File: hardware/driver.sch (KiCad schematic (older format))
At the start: 15 parts, among them Q1 BSS84, Q2 BSS138, Q3 BSS138, Q4 BSS84, Q5 BSS138, Q6 BSS138

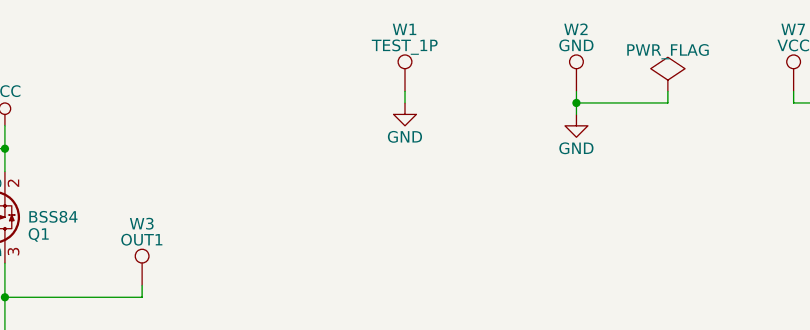
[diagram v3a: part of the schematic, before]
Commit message: Assigned footprints
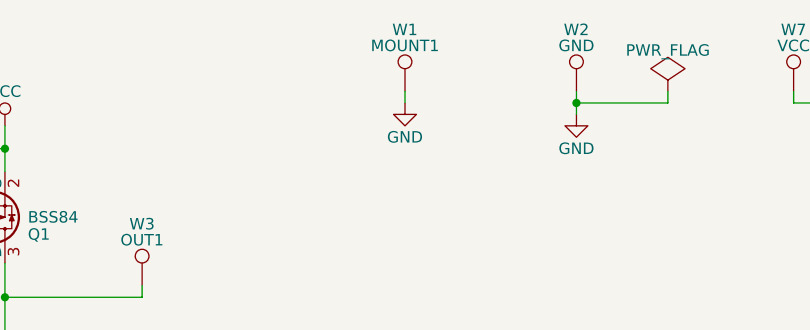
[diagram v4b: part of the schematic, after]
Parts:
- Q1, Q4: footprint (none) -> TO_SOT_Packages_SMD:SOT-23
- W1: value TEST_1P -> MOUNT1; footprint (none) -> Mounting_Holes:MountingHole_2.5mm_Pad
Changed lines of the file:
@@
 F 0 "Q1" H 4650 2175 50  0000 L CNN
 F 1 "BSS84" H 4650 2100 50  0000 L CNN
-F 2 "" H 4650 2025 50  0000 L CIN
+F 2 "TO_SOT_Packages_SMD:SOT-23" H 4650 2025 50  0001 L CIN
 F 3 "" H 4650 2175 50  0000 L CNN
 	1    4450 2100
@@
 F 0 "R1" V 3580 2150 50  0000 C CNN
 F 1 "R" V 3500 2150 50  0000 C CNN
-F 2 "" V 3430 2150 50  0000 C CNN
+F 2 "" V 3430 2150 50  0001 C CNN
 F 3 "" H 3500 2150 50  0000 C CNN
 	1    3500 2150
@@
 F 0 "W4" H 3000 3070 50  0000 C CNN
 F 1 "IN1" H 3000 3000 50  0000 C CNN
-F 2 "" H 3200 2800 50  0000 C CNN
+F 2 "" H 3200 2800 50  0001 C CNN
 F 3 "" H 3200 2800 50  0000 C CNN
 	1    3000 2800
@@
 F 0 "Q4" H 4650 4225 50  0000 L CNN
 F 1 "BSS84" H 4650 4150 50  0000 L CNN
-F 2 "" H 4650 4075 50  0000 L CIN
+F 2 "TO_SOT_Packages_SMD:SOT-23" H 4650 4075 50  0001 L CIN
 F 3 "" H 4650 4225 50  0000 L CNN
 	1    4450 4150
@@
 F 0 "R2" V 3580 4200 50  0000 C CNN
 F 1 "R" V 3500 4200 50  0000 C CNN
-F 2 "" V 3430 4200 50  0000 C CNN
+F 2 "" V 3430 4200 50  0001 C CNN
 F 3 "" H 3500 4200 50  0000 C CNN
 	1    3500 4200
@@
 F 0 "W6" H 3000 5120 50  0000 C CNN
 F 1 "IN2" H 3000 5050 50  0000 C CNN
-F 2 "" H 3200 4850 50  0000 C CNN
+F 2 "" H 3200 4850 50  0001 C CNN
 F 3 "" H 3200 4850 50  0000 C CNN
 	1    3000 4850
@@
 F 0 "W5" H 5150 4720 50  0000 C CNN
 F 1 "OUT2" H 5150 4650 50  0000 C CNN
-F 2 "" H 5350 4450 50  0000 C CNN
+F 2 "" H 5350 4450 50  0001 C CNN
 F 3 "" H 5350 4450 50  0000 C CNN
 	1    5150 4450
@@
 F 0 "W3" H 5150 2670 50  0000 C CNN
 F 1 "OUT1" H 5150 2600 50  0000 C CNN
-F 2 "" H 5350 2400 50  0000 C CNN
+F 2 "" H 5350 2400 50  0001 C CNN
 F 3 "" H 5350 2400 50  0000 C CNN
 	1    5150 2400
@@
 P 6300 1550
 F 0 "W1" H 6300 1820 50  0000 C CNN
-F 1 "TEST_1P" H 6300 1750 50  0000 C CNN
-F 2 "" H 6500 1550 50  0000 C CNN
+F 1 "MOUNT1" H 6300 1750 50  0000 C CNN
+F 2 "Mounting_Holes:MountingHole_2.5mm_Pad" H 6500 1550 50  0001 C CNN
 F 3 "" H 6500 1550 50  0000 C CNN
 	1    6300 1550
@@
 F 0 "W2" H 7050 1820 50  0000 C CNN
 F 1 "GND" H 7050 1750 50  0000 C CNN
-F 2 "" H 7250 1550 50  0000 C CNN
+F 2 "" H 7250 1550 50  0001 C CNN
 F 3 "" H 7250 1550 50  0000 C CNN
 	1    7050 1550
@@
 F 0 "W7" H 8000 1820 50  0000 C CNN
 F 1 "VCC" H 8000 1750 50  0000 C CNN
-F 2 "" H 8200 1550 50  0000 C CNN
+F 2 "" H 8200 1550 50  0001 C CNN
 F 3 "" H 8200 1550 50  0000 C CNN
 	1    8000 1550

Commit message: Initial PCB layout
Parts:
- R1, R2: footprint (none) -> Resistors_SMD:R_0603_HandSoldering
- W2, W3, W4, W5, W6, W7: footprint (none) -> Measurement_Points:Measurement_Point_Square-TH_Big
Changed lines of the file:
@@
 F 0 "R1" V 3580 2150 50  0000 C CNN
 F 1 "R" V 3500 2150 50  0000 C CNN
-F 2 "" V 3430 2150 50  0001 C CNN
+F 2 "Resistors_SMD:R_0603_HandSoldering" V 3430 2150 50  0001 C CNN
 F 3 "" H 3500 2150 50  0000 C CNN
 	1    3500 2150
@@
 F 0 "W4" H 3000 3070 50  0000 C CNN
 F 1 "IN1" H 3000 3000 50  0000 C CNN
-F 2 "" H 3200 2800 50  0001 C CNN
+F 2 "Measurement_Points:Measurement_Point_Square-TH_Big" H 3200 2800 50  0001 C CNN
 F 3 "" H 3200 2800 50  0000 C CNN
 	1    3000 2800
@@
 F 0 "R2" V 3580 4200 50  0000 C CNN
 F 1 "R" V 3500 4200 50  0000 C CNN
-F 2 "" V 3430 4200 50  0001 C CNN
+F 2 "Resistors_SMD:R_0603_HandSoldering" V 3430 4200 50  0001 C CNN
 F 3 "" H 3500 4200 50  0000 C CNN
 	1    3500 4200
@@
 F 0 "W6" H 3000 5120 50  0000 C CNN
 F 1 "IN2" H 3000 5050 50  0000 C CNN
-F 2 "" H 3200 4850 50  0001 C CNN
+F 2 "Measurement_Points:Measurement_Point_Square-TH_Big" H 3200 4850 50  0001 C CNN
 F 3 "" H 3200 4850 50  0000 C CNN
 	1    3000 4850
@@
 F 0 "W5" H 5150 4720 50  0000 C CNN
 F 1 "OUT2" H 5150 4650 50  0000 C CNN
-F 2 "" H 5350 4450 50  0001 C CNN
+F 2 "Measurement_Points:Measurement_Point_Square-TH_Big" H 5350 4450 50  0001 C CNN
 F 3 "" H 5350 4450 50  0000 C CNN
 	1    5150 4450
@@
 F 0 "W3" H 5150 2670 50  0000 C CNN
 F 1 "OUT1" H 5150 2600 50  0000 C CNN
-F 2 "" H 5350 2400 50  0001 C CNN
+F 2 "Measurement_Points:Measurement_Point_Square-TH_Big" H 5350 2400 50  0001 C CNN
 F 3 "" H 5350 2400 50  0000 C CNN
 	1    5150 2400
@@
 F 0 "W2" H 7050 1820 50  0000 C CNN
 F 1 "GND" H 7050 1750 50  0000 C CNN
-F 2 "" H 7250 1550 50  0001 C CNN
+F 2 "Measurement_Points:Measurement_Point_Square-TH_Big" H 7250 1550 50  0001 C CNN
 F 3 "" H 7250 1550 50  0000 C CNN
 	1    7050 1550
@@
 F 0 "W7" H 8000 1820 50  0000 C CNN
 F 1 "VCC" H 8000 1750 50  0000 C CNN
-F 2 "" H 8200 1550 50  0001 C CNN
+F 2 "Measurement_Points:Measurement_Point_Square-TH_Big" H 8200 1550 50  0001 C CNN
 F 3 "" H 8200 1550 50  0000 C CNN
 	1    8000 1550

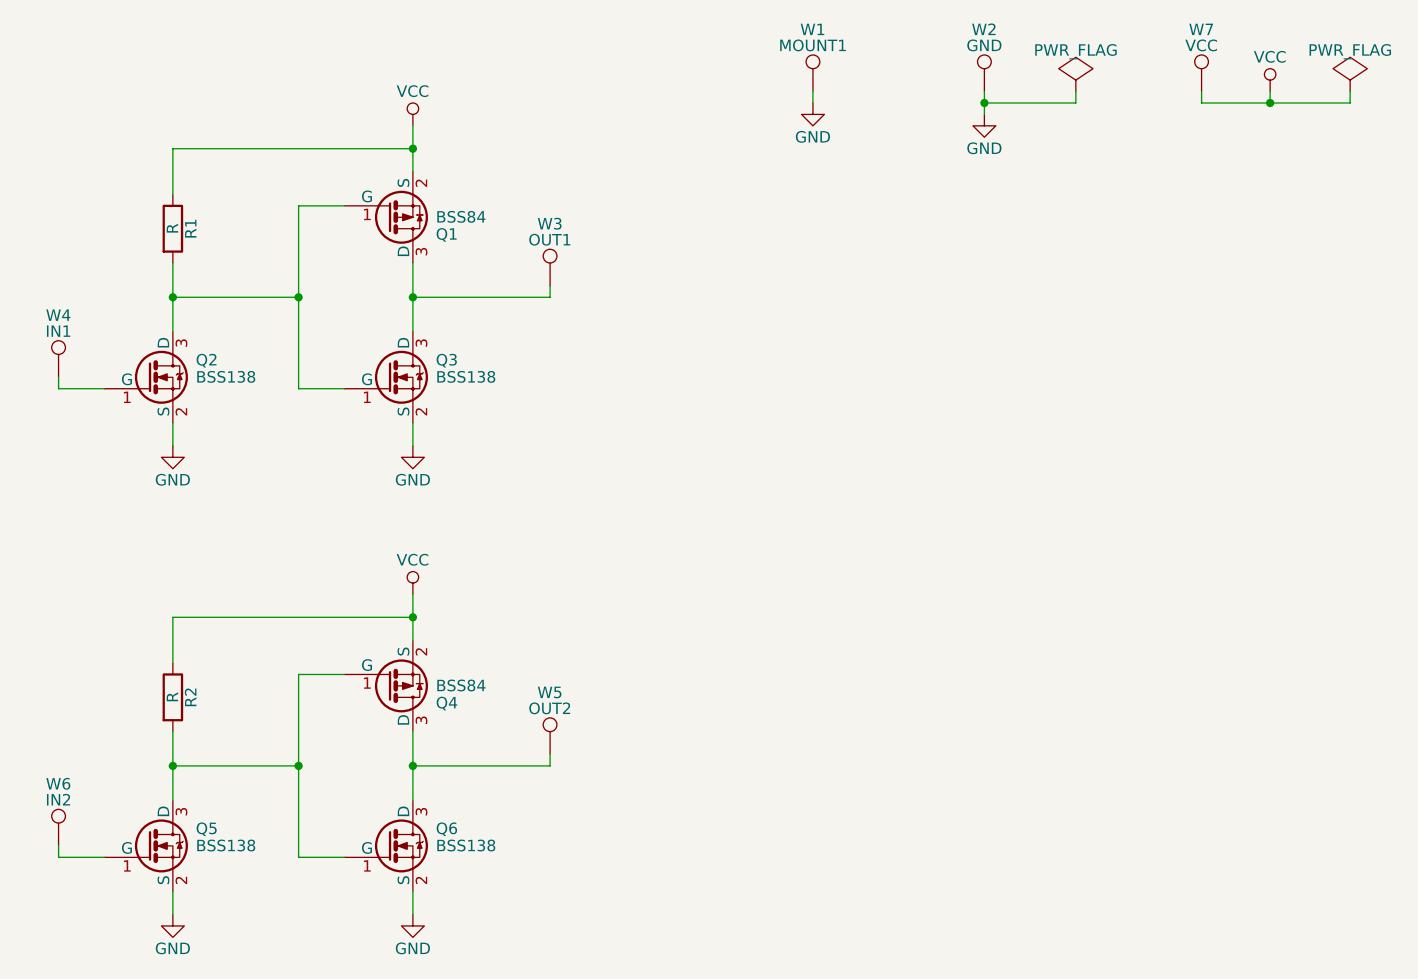
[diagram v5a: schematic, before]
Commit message: Added optional RC filter
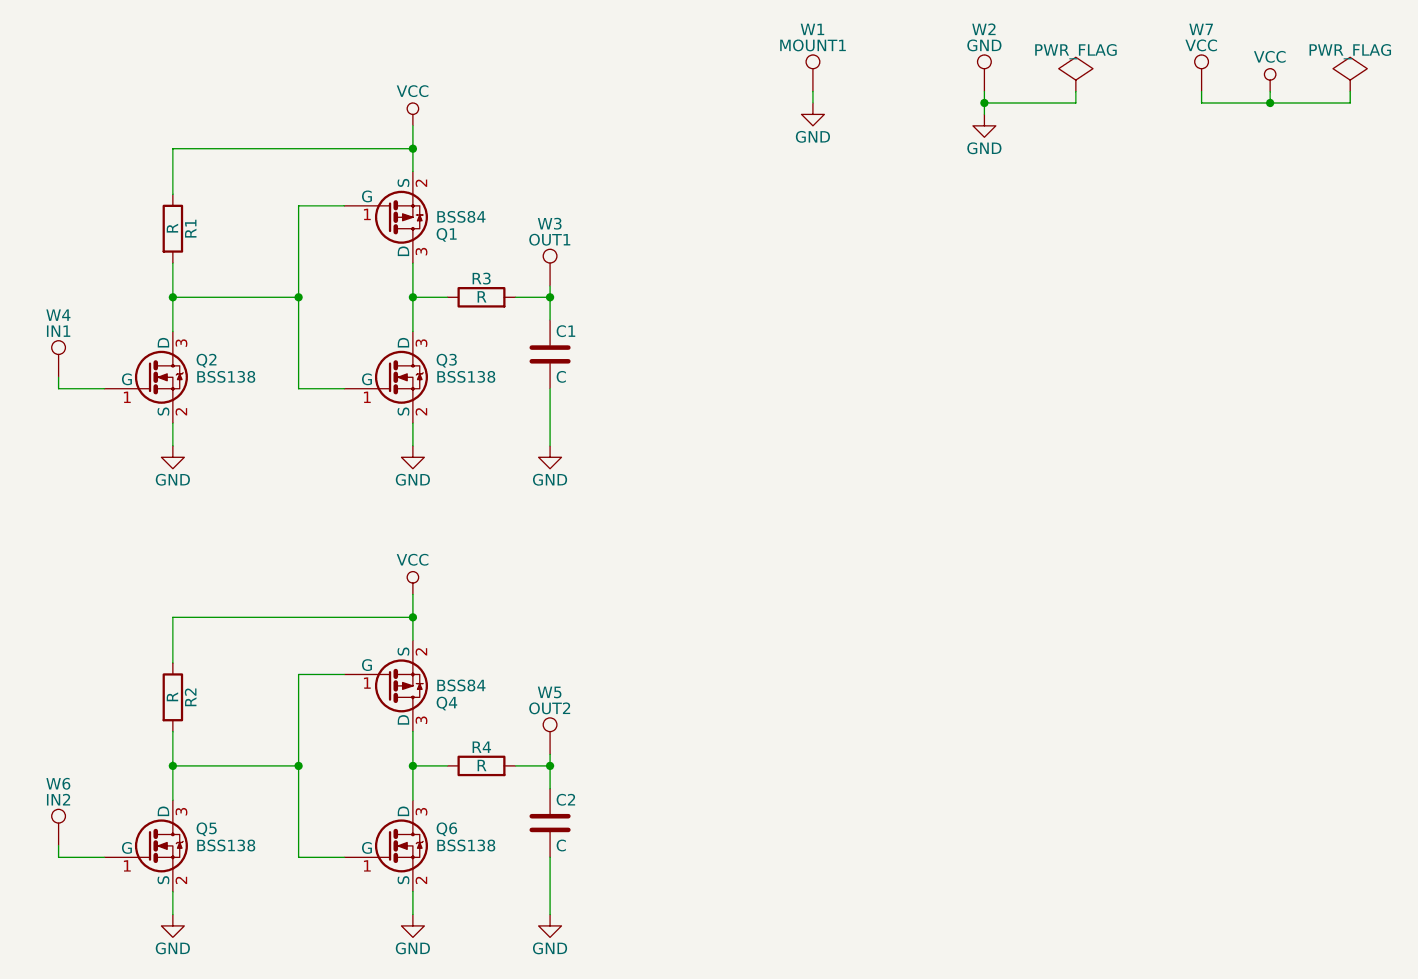
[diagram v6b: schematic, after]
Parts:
- added C1, C2: C, Capacitors_SMD:C_0603_HandSoldering, symbol C
- added R3, R4: R, Resistors_SMD:R_0603_HandSoldering, symbol R
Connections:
- net GND: now also C1.2, C2.2
- net at Q1.3 (D), Q3.3 (D): now also R3.1; no longer W3.1
- net at Q4.3 (D), Q6.3 (D): now also R4.1; no longer W5.1
- new net: C2.1, R4.2, W5.1
- new net: C1.1, R3.2, W3.1
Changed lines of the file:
@@
 Connection ~ 4050 2450
 Connection ~ 3500 2450
-Wire Wire Line
-	4550 2450 5150 2450
 Connection ~ 4550 2450
 Wire Wire Line
@@
 	1    0    0    1
 $EndComp
-Wire Wire Line
-	4550 4500 5150 4500
 Connection ~ 4550 4500
 $Comp
@@
 $EndComp
 Wire Wire Line
-	5150 2450 5150 2400
-Wire Wire Line
-	5150 4500 5150 4450
+	5150 2400 5150 2550
+Wire Wire Line
+	5150 4450 5150 4600
 Wire Wire Line
 	4550 2300 4550 2600
@@
 	7450 1600 7450 1550
 Connection ~ 7050 1600
+$Comp
+L R R3
+U 1 1 58938045
+P 4850 2450
+F 0 "R3" V 4930 2450 50  0000 C CNN
+F 1 "R" V 4850 2450 50  0000 C CNN
+F 2 "Resistors_SMD:R_0603_HandSoldering" V 4780 2450 50  0001 C CNN
+F 3 "" H 4850 2450 50  0000 C CNN
+	1    4850 2450
+	0    -1   -1   0
+$EndComp
+Wire Wire Line
+	4550 2450 4700 2450
+Wire Wire Line
+	5000 2450 5150 2450
+$Comp
+L R R4
+U 1 1 58938378
+P 4850 4500
+F 0 "R4" V 4930 4500 50  0000 C CNN
+F 1 "R" V 4850 4500 50  0000 C CNN
+F 2 "Resistors_SMD:R_0603_HandSoldering" V 4780 4500 50  0001 C CNN
+F 3 "" H 4850 4500 50  0000 C CNN
+	1    4850 4500
+	0    -1   -1   0
+$EndComp
+Wire Wire Line
+	4700 4500 4550 4500
+Wire Wire Line
+	5000 4500 5150 4500
+$Comp
+L C C1
+U 1 1 58938479
+P 5150 2700
+F 0 "C1" H 5175 2800 50  0000 L CNN
+F 1 "C" H 5175 2600 50  0000 L CNN
+F 2 "Capacitors_SMD:C_0603_HandSoldering" H 5188 2550 50  0001 C CNN
+F 3 "" H 5150 2700 50  0000 C CNN
+	1    5150 2700
+	1    0    0    -1
+$EndComp
+$Comp
+L C C2
+U 1 1 589389FC
+P 5150 4750
+F 0 "C2" H 5175 4850 50  0000 L CNN
+F 1 "C" H 5175 4650 50  0000 L CNN
+F 2 "Capacitors_SMD:C_0603_HandSoldering" H 5188 4600 50  0001 C CNN
+F 3 "" H 5150 4750 50  0000 C CNN
+	1    5150 4750
+	1    0    0    -1
+$EndComp
+Connection ~ 5150 2450
+$Comp
+L GND #PWR012
+U 1 1 589397B2
+P 5150 3100
+F 0 "#PWR012" H 5150 2850 50  0001 C CNN
+F 1 "GND" H 5150 2950 50  0000 C CNN
+F 2 "" H 5150 3100 50  0000 C CNN
+F 3 "" H 5150 3100 50  0000 C CNN
+	1    5150 3100
+	1    0    0    -1
+$EndComp
+Wire Wire Line
+	5150 2850 5150 3100
+Connection ~ 5150 4500
+Wire Wire Line
+	5150 4900 5150 5150
+$Comp
+L GND #PWR013
+U 1 1 58939E89
+P 5150 5150
+F 0 "#PWR013" H 5150 4900 50  0001 C CNN
+F 1 "GND" H 5150 5000 50  0000 C CNN
+F 2 "" H 5150 5150 50  0000 C CNN
+F 3 "" H 5150 5150 50  0000 C CNN
+	1    5150 5150
+	1    0    0    -1
+$EndComp
 $EndSCHEMATC
